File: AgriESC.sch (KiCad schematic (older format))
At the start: 129 parts, among them J1 SUPPLY, J10 GPIO, J11 USB_OTG, J12 HALL_ENC, J2 PH_A, J3 PH_B, J4 PH_C, J5 GND, J6 COMM, J7 SERVO, J8 CAN, J9 SWD, SW1 SW_SPDT, U1 FDMS7698, U10 STM32F405RGT6, U11 DRV8303, U12 TJA1051TK-3, U13 LMR16006YQ, U14 MCP1700-3302E_SOT23, U15 MCP1700-3302E_SOT23, U2 FDMS7698, U3 FDMS7698, U4 FDMS7698, U5 FDMS7698, U6 FDMS7698, U7 MAX9920, U8 MAX9920, U9 MAX9920, Y1 8M_15p_capacitance

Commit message: Created draft net
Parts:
- J1, J2, J3, J4, J5: footprint (none) -> Connector_Wire:SolderWirePad_1x01_SMD_5x10mm
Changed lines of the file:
@@
 F 0 "J2" H 820 -1625 50  0000 C CNN
 F 1 "PH_A" H 820 -1534 50  0000 C CNN
-F 2 "" H 900 -1400 50  0001 C CNN
+F 2 "Connector_Wire:SolderWirePad_1x01_SMD_5x10mm" H 900 -1400 50  0001 C CNN
 F 3 "~" H 900 -1400 50  0001 C CNN
 	1    900  -1400
@@
 F 0 "J3" H 4120 -1625 50  0000 C CNN
 F 1 "PH_B" H 4120 -1534 50  0000 C CNN
-F 2 "" H 4200 -1400 50  0001 C CNN
+F 2 "Connector_Wire:SolderWirePad_1x01_SMD_5x10mm" H 4200 -1400 50  0001 C CNN
 F 3 "~" H 4200 -1400 50  0001 C CNN
 	1    4200 -1400
@@
 F 0 "J4" H 7370 -1625 50  0000 C CNN
 F 1 "PH_C" H 7370 -1534 50  0000 C CNN
-F 2 "" H 7450 -1400 50  0001 C CNN
+F 2 "Connector_Wire:SolderWirePad_1x01_SMD_5x10mm" H 7450 -1400 50  0001 C CNN
 F 3 "~" H 7450 -1400 50  0001 C CNN
 	1    7450 -1400
@@
 F 0 "J1" H 10330 -2308 50  0000 L CNN
 F 1 "SUPPLY" H 10330 -2399 50  0000 L CNN
-F 2 "" H 10250 -2350 50  0001 C CNN
+F 2 "Connector_Wire:SolderWirePad_1x01_SMD_5x10mm" H 10250 -2350 50  0001 C CNN
 F 3 "~" H 10250 -2350 50  0001 C CNN
 	1    10250 -2350
@@
 F 0 "J5" H 10329 -158 50  0000 L CNN
 F 1 "GND" H 10329 -249 50  0000 L CNN
-F 2 "" H 10250 -200 50  0001 C CNN
+F 2 "Connector_Wire:SolderWirePad_1x01_SMD_5x10mm" H 10250 -200 50  0001 C CNN
 F 3 "~" H 10250 -200 50  0001 C CNN
 	1    10250 -200

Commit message: Updated schematic with new battery supply connector and more MPNs
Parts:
- removed J1: SUPPLY, Connector_Wire:SolderWirePad_1x01_SMD_5x10mm, symbol Connector_Generic:Conn_01x01
- removed J5: GND, Connector_Wire:SolderWirePad_1x01_SMD_5x10mm, symbol Connector_Generic:Conn_01x01
- removed Y1: 8M_15p_capacitance, Crystal:Crystal_HC49-U_Vertical, symbol Device:Crystal_GND3
- added J1: SUPPLY, AgriESC:XT30PW-M2, symbol Connector_Generic:Conn_01x02
- added Y1: 8M_15p_capacitance, Crystal:Crystal_HC49-U_Vertical, symbol Device:Crystal
- C10, C11, C12, C13, C14, C15, C16, C17, C18, C19, C20, C21, C22, C23, C24, C25, C26, C27, C28, C29, C30, C31, C32, C33, C34, C35, C36, C37, C38, C39, C40, C42, C43, C44, C45, C46, C48, C49, C50, C51, C52, C9: footprint Capacitor_SMD:C_0805_2012Metric_Pad1.15x1.40mm_HandSolder -> Capacitor_SMD:C_0603_1608Metric_Pad1.05x0.95mm_HandSolder
- C47: value 2u2_30V -> 2u2_35V; footprint Capacitor_SMD:C_0805_2012Metric_Pad1.15x1.40mm_HandSolder -> Capacitor_SMD:C_0603_1608Metric_Pad1.05x0.95mm_HandSolder
- D1, D2, D3: footprint LED_SMD:LED_0805_2012Metric_Pad1.15x1.40mm_HandSolder -> LED_SMD:LED_0603_1608Metric_Pad1.05x0.95mm_HandSolder
- J10, J12: footprint Connector_PinHeader_2.54mm:PinHeader_1x06_P2.54mm_Vertical -> AgriESC:JST_PA_01x06
- J11: footprint Connector_USB:USB_Micro-B_Amphenol_10103594-0001LF_Horizontal -> AgriESC:CONN-10118194-0001LF-FCI2
- J6: footprint Connector_PinHeader_2.54mm:PinHeader_1x08_P2.54mm_Vertical -> AgriESC:JST_PA_01x08
- J7: footprint Connector_PinHeader_2.54mm:PinHeader_1x03_P2.54mm_Vertical -> AgriESC:JST_PA_01x03
- J8: footprint Connector_PinHeader_2.54mm:PinHeader_1x04_P2.54mm_Vertical -> AgriESC:JST_PA_01x04
- J9: footprint Connector_PinHeader_2.54mm:PinHeader_1x05_P2.54mm_Vertical -> AgriESC:JST_PA_01x05
- R1, R10, R11, R12, R13, R14, R15, R16, R17, R18, R19, R2, R20, R21, R22, R23, R24, R25, R26, R27, R28, R29, R3, R30, R31, R32, R33, R34, R35, R36, R37, R38, R39, R40, R41, R42, R43, R7, R8, R9: footprint Resistor_SMD:R_0805_2012Metric_Pad1.15x1.40mm_HandSolder -> Resistor_SMD:R_0603_1608Metric_Pad1.05x0.95mm_HandSolder
- SW1: footprint AgriESC:1825232-1 -> Jumper:SolderJumper-3_P1.3mm_Open_RoundedPad1.0x1.5mm_NumberLabels
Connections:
- wire segments 595 -> 596
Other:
- note added: "35PX680MEFC10X16"
- note removed: "1825232-1"
- moved on the sheet: C46, C47, C48, C49, C50, C51, C52, D4, L1, R41, R42, R43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

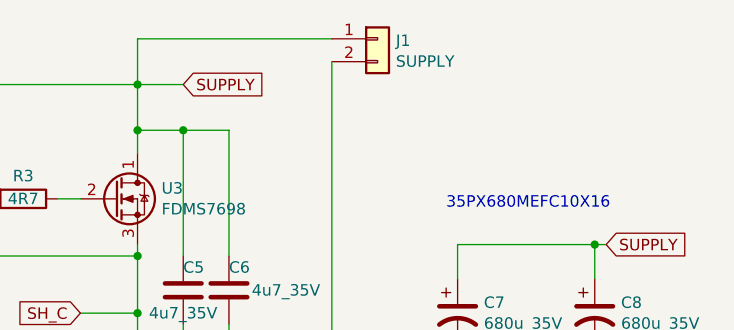
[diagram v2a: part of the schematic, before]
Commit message: Corrected battery connector polarity
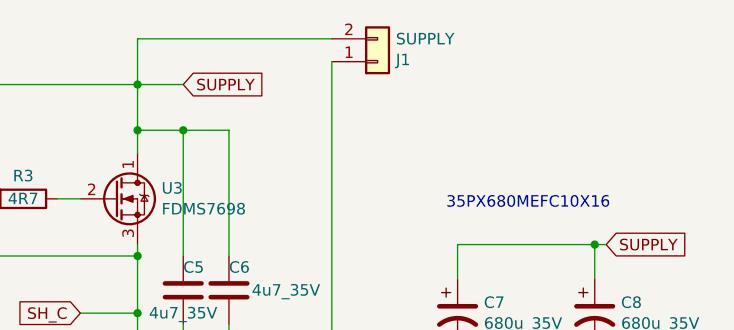
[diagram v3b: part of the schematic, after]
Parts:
- J1: footprint AgriESC:XT30PW-M2 -> AgriESC:XT30PW-F
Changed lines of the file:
@@
 L Connector_Generic:Conn_01x02 J1
 U 1 1 5C7BF897
-P 10900 -2350
-F 0 "J1" H 10980 -2358 50  0000 L CNN
-F 1 "SUPPLY" H 10980 -2449 50  0000 L CNN
-F 2 "AgriESC:XT30PW-M2" H 10900 -2350 50  0001 C CNN
-F 3 "~" H 10900 -2350 50  0001 C CNN
-	1    10900 -2350
-	1    0    0    -1
+P 10900 -2250
+F 0 "J1" H 10980 -2258 50  0000 L CNN
+F 1 "SUPPLY" H 10980 -2349 50  0000 L CNN
+F 2 "AgriESC:XT30PW-F" H 10900 -2250 50  0001 C CNN
+F 3 "~" H 10900 -2250 50  0001 C CNN
+	1    10900 -2250
+	1    0    0    1
 $EndComp
 Wire Wire Line

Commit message: Updated schematic with new components
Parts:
- removed Y1: 8M_15p_capacitance, Crystal:Crystal_HC49-U_Vertical, symbol Device:Crystal
- added Y1: 8M Resonator, AgriESC:CSTNE8M00G550000R0, symbol Device:Resonator
- L1: footprint Inductor_THT:L_Radial_D9.5mm_P5.00mm_Fastron_07HVP -> AgriESC:NR8040T220M
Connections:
- wire segments 596 -> 597
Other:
- note added: "CSTNE8M00G550000R0"
- note added: "NR8040T220M"
- note removed: "FC4STCBAF8.0-BAG200"
- note removed: "LHL08TB220K"
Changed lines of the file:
@@
 F 0 "L1" V 4490 9050 50  0000 C CNN
 F 1 "22u" V 4399 9050 50  0000 C CNN
-F 2 "Inductor_THT:L_Radial_D9.5mm_P5.00mm_Fastron_07HVP" H 4300 9050 50  0001 C CNN
+F 2 "AgriESC:NR8040T220M" H 4300 9050 50  0001 C CNN
 F 3 "~" H 4300 9050 50  0001 C CNN
 	1    4300 9050
@@
 $EndComp
 Text Notes 6550 2550 0    50   ~ 0
-FC4STCBAF8.0-BAG200
+CSTNE8M00G550000R0
 Text Notes 4100 8700 0    50   ~ 0
-LHL08TB220K
-$Comp
-L Device:Crystal Y1
-U 1 1 5C747901
-P 7000 2900
-F 0 "Y1" H 7000 3168 50  0000 C CNN
-F 1 "8M_15p_capacitance" H 7000 3077 50  0000 C CNN
-F 2 "Crystal:Crystal_HC49-U_Vertical" H 7000 2900 50  0001 C CNN
-F 3 "~" H 7000 2900 50  0001 C CNN
-	1    7000 2900
-	1    0    0    -1
-$EndComp
+NR8040T220M
 Text Notes 11200 -1600 0    50   ~ 0
 35PX680MEFC10X16
@@
 	10700 -200 10050 -200
 Connection ~ 10050 -200
+$Comp
+L Device:Resonator Y1
+U 1 1 5B759714
+P 7000 2900
+F 0 "Y1" H 7000 3148 50  0000 C CNN
+F 1 "8M Resonator" H 7000 3057 50  0000 C CNN
+F 2 "AgriESC:CSTNE8M00G550000R0" H 6975 2900 50  0001 C CNN
+F 3 "~" H 6975 2900 50  0001 C CNN
+	1    7000 2900
+	1    0    0    -1
+$EndComp
+$Comp
+L power:GND #PWR0101
+U 1 1 5B759B20
+P 7000 3150
+F 0 "#PWR0101" H 7000 2900 50  0001 C CNN
+F 1 "GND" H 7005 2977 50  0000 C CNN
+F 2 "" H 7000 3150 50  0001 C CNN
+F 3 "" H 7000 3150 50  0001 C CNN
+	1    7000 3150
+	1    0    0    -1
+$EndComp
+Wire Wire Line
+	7000 3100 7000 3150
 $EndSCHEMATC

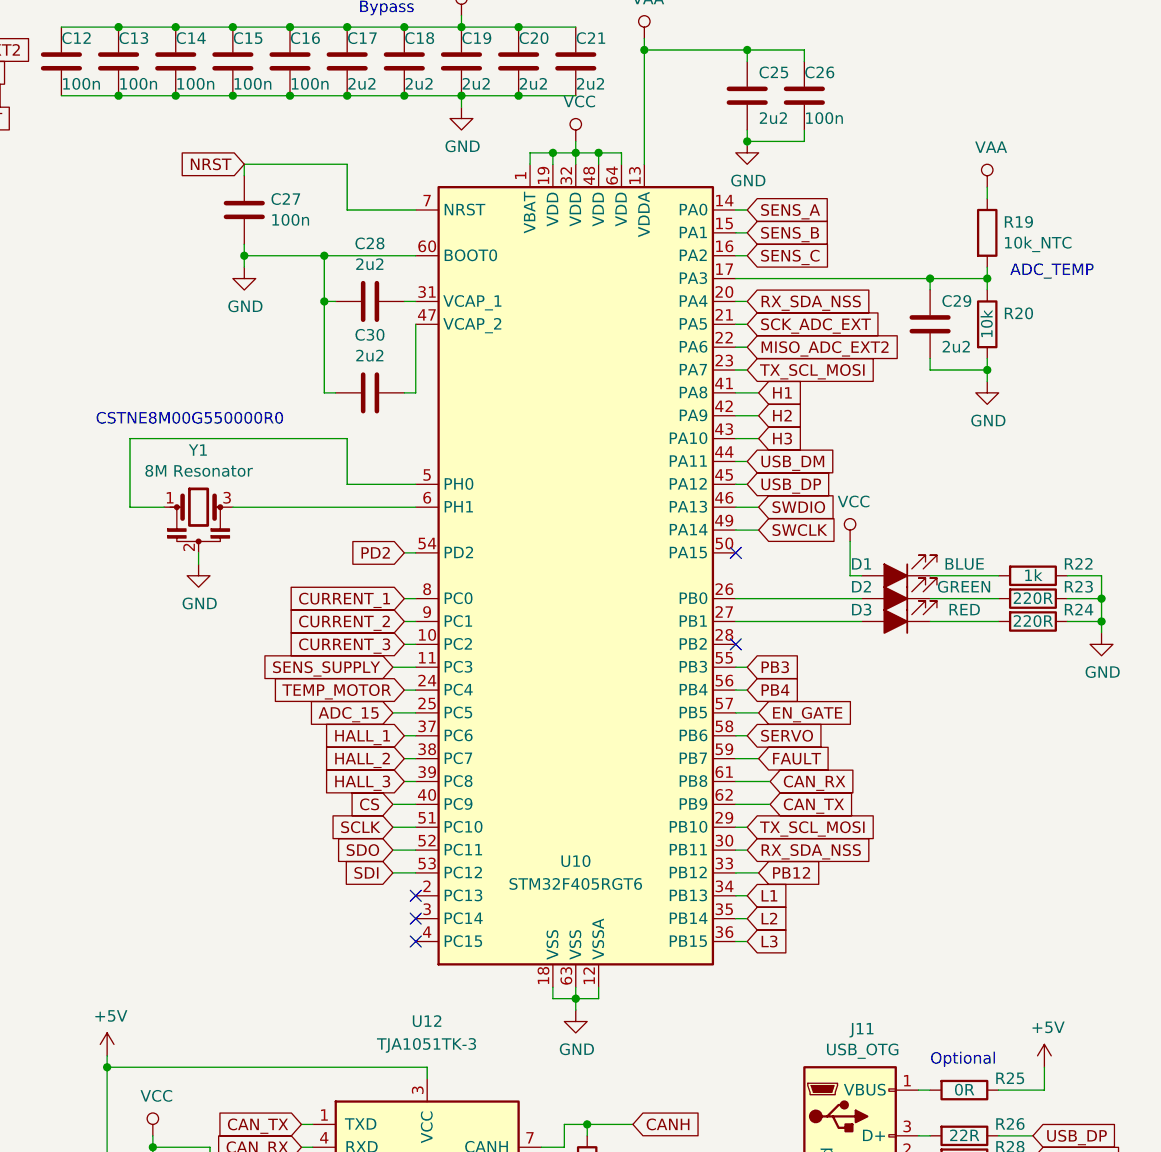
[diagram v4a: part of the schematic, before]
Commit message: Updated resonator footprint to include silkscreen
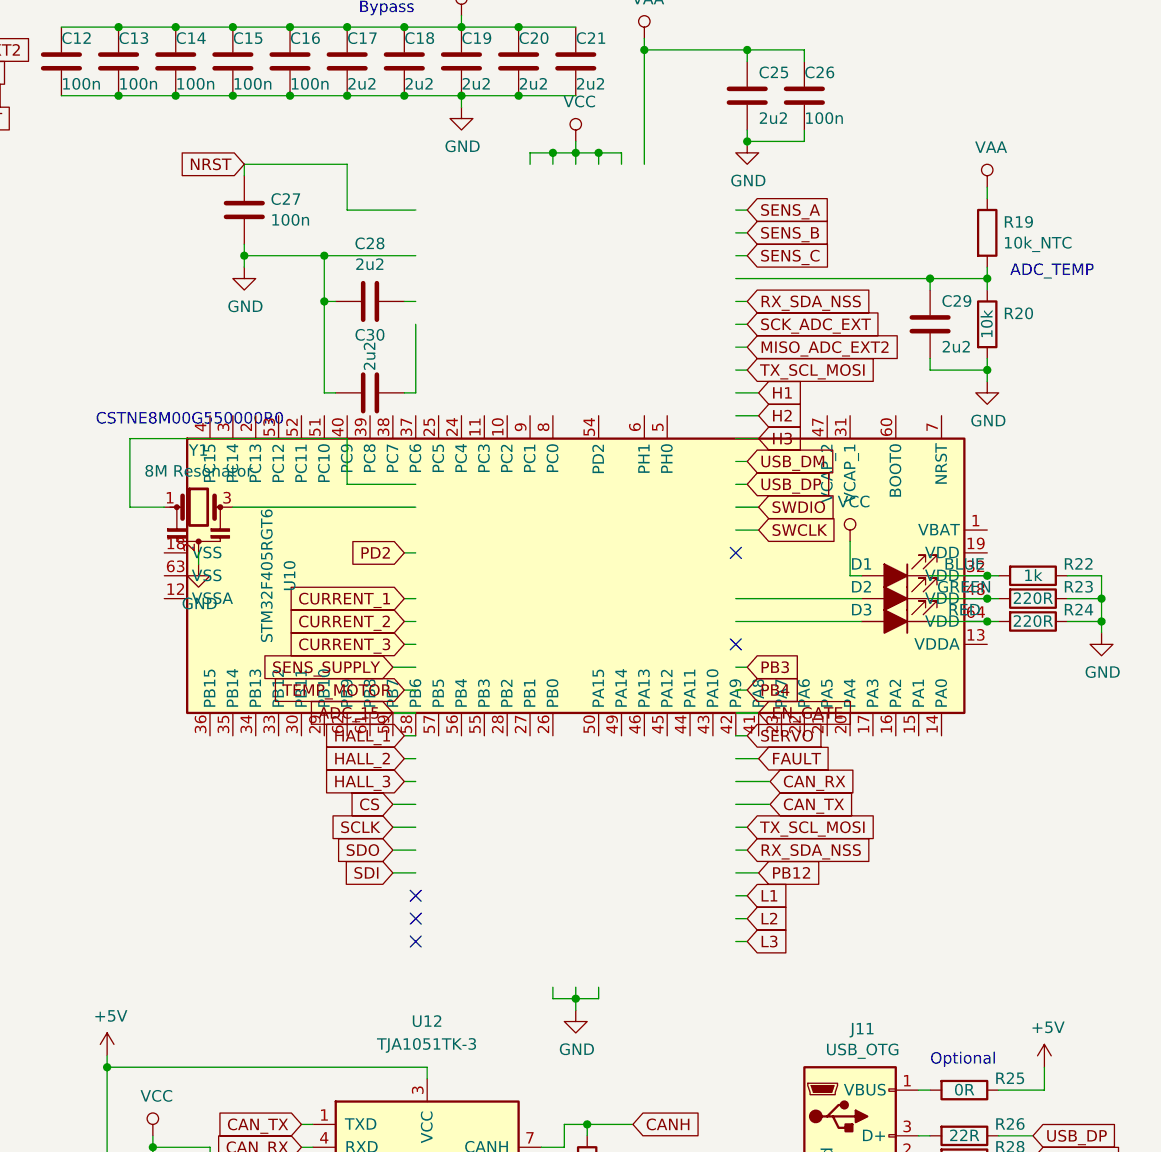
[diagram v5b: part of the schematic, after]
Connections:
- wire segments 597 -> 600
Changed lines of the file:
@@
 F 3 "http://www.st.com/st-web-ui/static/active/en/resource/technical/document/datasheet/DM00037051.pdf" H 8650 3200 50  0001 C CNN
 	1    8650 3200
-	1    0    0    -1
+	0    1    1    0
 $EndComp
 Wire Wire Line
@@
 P 7750 2400
 F 0 "C30" V 7498 2400 50  0000 C CNN
-F 1 "2u2" V 7589 2400 50  0000 C CNN
+F 1 "2u2" H 7589 2400 50  0000 C CNN
 F 2 "Capacitor_SMD:C_0603_1608Metric_Pad1.05x0.95mm_HandSolder" H 7788 2250 50  0001 C CNN
 F 3 "~" H 7750 2400 50  0001 C CNN
@@
 	9850 3200 9900 3200
 Wire Wire Line
-	10500 3200 10200 3200
+	10500 3200 10450 3200
 Wire Wire Line
 	9350 3300 9900 3300
@@
 $EndComp
 Wire Wire Line
-	10500 3300 10200 3300
+	10500 3300 10450 3300
 Wire Wire Line
-	10200 3400 10500 3400
+	10200 3400 10450 3400
 Wire Wire Line
 	10800 3200 10950 3200
@@
 Wire Wire Line
 	7000 3100 7000 3150
+Connection ~ 10450 3200
+Wire Wire Line
+	10450 3200 10200 3200
+Connection ~ 10450 3300
+Wire Wire Line
+	10450 3300 10200 3300
+Connection ~ 10450 3400
+Wire Wire Line
+	10450 3400 10500 3400
 $EndSCHEMATC

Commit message: Fix to schematic
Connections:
- wire segments 600 -> 597
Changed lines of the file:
@@
 F 3 "http://www.st.com/st-web-ui/static/active/en/resource/technical/document/datasheet/DM00037051.pdf" H 8650 3200 50  0001 C CNN
 	1    8650 3200
-	0    1    1    0
+	1    0    0    -1
 $EndComp
 Wire Wire Line
@@
 	9450 2400 9350 2400
 Wire Wire Line
-	9350 2500 9450 2500
-Wire Wire Line
 	9350 2600 9450 2600
 Text GLabel 9400 2700 2    50   Input ~ 0
@@
 	7950 2000 7900 2000
 Wire Wire Line
-	7950 2100 7950 2400
-Wire Wire Line
 	7950 2400 7900 2400
 Wire Wire Line
@@
 	9850 3200 9900 3200
 Wire Wire Line
-	10500 3200 10450 3200
-Wire Wire Line
 	9350 3300 9900 3300
 Wire Wire Line
@@
 $EndComp
 Wire Wire Line
-	10500 3300 10450 3300
-Wire Wire Line
-	10200 3400 10450 3400
-Wire Wire Line
 	10800 3200 10950 3200
 Wire Wire Line
@@
 Wire Wire Line
 	7000 3100 7000 3150
-Connection ~ 10450 3200
 Wire Wire Line
-	10450 3200 10200 3200
-Connection ~ 10450 3300
+	9350 2500 9450 2500
+Wire Wire Line
+	7950 2100 7950 2400
+Wire Wire Line
+	10200 3400 10500 3400
 Wire Wire Line
-	10450 3300 10200 3300
-Connection ~ 10450 3400
+	10200 3300 10500 3300
 Wire Wire Line
-	10450 3400 10500 3400
+	10200 3200 10500 3200
 $EndSCHEMATC

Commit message: Before CAN package update
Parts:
- U12: footprint Package_DFN_QFN:DFN-8-1EP_3x3mm_P0.65mm_EP1.55x2.4mm -> Housings_DFN_QFN:DFN-8-1EP_3x3mm_Pitch0.65mm
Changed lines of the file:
@@
 EESchema Schematic File Version 4
 LIBS:AgriESC-cache
-EELAYER 26 0
+EELAYER 29 0
 EELAYER END
 $Descr A4 11693 8268
@@
 F 0 "U12" H 8000 6450 50  0000 C CNN
 F 1 "TJA1051TK-3" H 8000 6350 50  0000 C CNN
-F 2 "Package_DFN_QFN:DFN-8-1EP_3x3mm_P0.65mm_EP1.55x2.4mm" H 8000 5300 50  0001 C CIN
+F 2 "Housings_DFN_QFN:DFN-8-1EP_3x3mm_Pitch0.65mm" H 8000 5300 50  0001 C CIN
 F 3 "http://www.nxp.com/documents/data_sheet/TJA1051.pdf" H 8000 5800 50  0001 C CNN
 	1    8000 5800

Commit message: Version 1.0 completed
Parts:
- added NT1, NT2, NT3: Net-Tie_2, NetTie:NetTie-2_SMD_Pad0.5mm, symbol Device:Net-Tie_2
- C7, C8: footprint Capacitor_THT:CP_Radial_D10.0mm_P5.00mm -> AgriESC:CP_Radial_D10.0mm_P5.00mm_Side_Mounted
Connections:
- net GND: now also NT1.1, NT2.1, NT3.1; no longer U11.30 (SL_C), U11.35 (SL_B), U11.40 (SL_A)
- net VCC: now also J12.6 (Pin_6), R33.2, R34.2, R37.2, SW1.2 (B)
- new net SL_A: NT1.2, U11.40 (SL_A)
- new net SL_B: NT2.2, U11.35 (SL_B)
- new net SL_C: NT3.2, U11.30 (SL_C)
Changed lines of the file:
@@
 EESchema Schematic File Version 4
 LIBS:AgriESC-cache
-EELAYER 29 0
+EELAYER 26 0
 EELAYER END
 $Descr A4 11693 8268
@@
 SL_A
 Wire Wire Line
-	3050 -450 3300 -450
-Wire Wire Line
 	3300 -450 3300 -600
 $Comp
@@
 	3300 -1950 3300 -2150
 Connection ~ 3300 -1950
-Wire Wire Line
-	3300 -450 3300 -200
 Text GLabel 2500 -1650 0    50   Input ~ 0
 GH_A
@@
 SL_B
 Wire Wire Line
-	6350 -450 6600 -450
-Wire Wire Line
 	6600 -450 6600 -600
 $Comp
@@
 	6600 -1950 6600 -2150
 Connection ~ 6600 -1950
-Wire Wire Line
-	6600 -450 6600 -200
 Text GLabel 5800 -1650 0    50   Input ~ 0
 GH_B
@@
 SL_C
 Wire Wire Line
-	9600 -450 9850 -450
-Wire Wire Line
 	9850 -450 9850 -600
 $Comp
@@
 	9850 -2350 9850 -2150
 Wire Wire Line
-	3300 -200 6600 -200
-Connection ~ 6600 -200
-Wire Wire Line
-	9850 -450 9850 -200
-Wire Wire Line
 	10050 -200 10050 -50
-Connection ~ 9850 -200
-Wire Wire Line
-	9850 -200 10050 -200
-Wire Wire Line
-	6600 -200 9850 -200
 Text GLabel 1050 800  0    50   Input ~ 0
 CURRENT_1
@@
 L power:PWR_FLAG #FLG01
 U 1 1 5E04539D
-P 2650 6800
-F 0 "#FLG01" H 2650 6875 50  0001 C CNN
-F 1 "PWR_FLAG" H 2650 6974 50  0000 C CNN
-F 2 "" H 2650 6800 50  0001 C CNN
-F 3 "~" H 2650 6800 50  0001 C CNN
-	1    2650 6800
+P 2700 6200
+F 0 "#FLG01" H 2700 6275 50  0001 C CNN
+F 1 "PWR_FLAG" H 2700 6374 50  0000 C CNN
+F 2 "" H 2700 6200 50  0001 C CNN
+F 3 "~" H 2700 6200 50  0001 C CNN
+	1    2700 6200
 	1    0    0    -1
 $EndComp
@@
 L power:GND #PWR055
 U 1 1 5E045557
-P 2650 6850
-F 0 "#PWR055" H 2650 6600 50  0001 C CNN
-F 1 "GND" H 2655 6677 50  0000 C CNN
-F 2 "" H 2650 6850 50  0001 C CNN
-F 3 "" H 2650 6850 50  0001 C CNN
-	1    2650 6850
+P 2700 6250
+F 0 "#PWR055" H 2700 6000 50  0001 C CNN
+F 1 "GND" H 2705 6077 50  0000 C CNN
+F 2 "" H 2700 6250 50  0001 C CNN
+F 3 "" H 2700 6250 50  0001 C CNN
+	1    2700 6250
 	1    0    0    -1
 $EndComp
@@
 L power:PWR_FLAG #FLG02
 U 1 1 5E0457CD
-P 3000 6850
-F 0 "#FLG02" H 3000 6925 50  0001 C CNN
-F 1 "PWR_FLAG" H 3000 7023 50  0000 C CNN
-F 2 "" H 3000 6850 50  0001 C CNN
-F 3 "~" H 3000 6850 50  0001 C CNN
-	1    3000 6850
+P 3050 6250
+F 0 "#FLG02" H 3050 6325 50  0001 C CNN
+F 1 "PWR_FLAG" H 3050 6423 50  0000 C CNN
+F 2 "" H 3050 6250 50  0001 C CNN
+F 3 "~" H 3050 6250 50  0001 C CNN
+	1    3050 6250
 	-1   0    0    1
 $EndComp
@@
 L power:+5V #PWR054
 U 1 1 5E045EB9
-P 3000 6800
-F 0 "#PWR054" H 3000 6650 50  0001 C CNN
-F 1 "+5V" H 3015 6973 50  0000 C CNN
-F 2 "" H 3000 6800 50  0001 C CNN
-F 3 "" H 3000 6800 50  0001 C CNN
-	1    3000 6800
+P 3050 6200
+F 0 "#PWR054" H 3050 6050 50  0001 C CNN
+F 1 "+5V" H 3065 6373 50  0000 C CNN
+F 2 "" H 3050 6200 50  0001 C CNN
+F 3 "" H 3050 6200 50  0001 C CNN
+	1    3050 6200
 	1    0    0    -1
 $EndComp
 Wire Wire Line
-	3000 6800 3000 6850
+	3050 6200 3050 6250
 Wire Wire Line
-	2650 6800 2650 6850
+	2700 6200 2700 6250
 Text GLabel 1850 8850 0    50   Input ~ 0
 SUPPLY
@@
 L power:PWR_FLAG #FLG03
 U 1 1 5E1F88B7
-P 3400 6850
-F 0 "#FLG03" H 3400 6925 50  0001 C CNN
-F 1 "PWR_FLAG" H 3400 7023 50  0000 C CNN
-F 2 "" H 3400 6850 50  0001 C CNN
-F 3 "~" H 3400 6850 50  0001 C CNN
-	1    3400 6850
+P 2700 7050
+F 0 "#FLG03" H 2700 7125 50  0001 C CNN
+F 1 "PWR_FLAG" H 2700 7223 50  0000 C CNN
+F 2 "" H 2700 7050 50  0001 C CNN
+F 3 "~" H 2700 7050 50  0001 C CNN
+	1    2700 7050
 	-1   0    0    1
 $EndComp
-Text GLabel 3400 6800 1    50   Input ~ 0
+Text GLabel 2700 7000 1    50   Input ~ 0
 SUPPLY
 Wire Wire Line
-	3400 6800 3400 6850
+	2700 7000 2700 7050
 Text Notes 2550 9900 0    50   ~ 0
 From the design guide
@@
 F 0 "C7" H 11365 -1104 50  0000 L CNN
 F 1 "680u_35V" H 11365 -1195 50  0000 L CNN
-F 2 "Capacitor_THT:CP_Radial_D10.0mm_P5.00mm" H 11250 -1150 50  0001 C CNN
+F 2 "AgriESC:CP_Radial_D10.0mm_P5.00mm_Side_Mounted" H 11250 -1150 50  0001 C CNN
 F 3 "~" H 11250 -1150 50  0001 C CNN
 	1    11250 -1150
@@
 F 0 "C8" H 11965 -1104 50  0000 L CNN
 F 1 "680u_35V" H 11965 -1195 50  0000 L CNN
-F 2 "Capacitor_THT:CP_Radial_D10.0mm_P5.00mm" H 11850 -1150 50  0001 C CNN
+F 2 "AgriESC:CP_Radial_D10.0mm_P5.00mm_Side_Mounted" H 11850 -1150 50  0001 C CNN
 F 3 "~" H 11850 -1150 50  0001 C CNN
 	1    11850 -1150
@@
 Wire Wire Line
 	10200 3200 10500 3200
+$Comp
+L Device:Net-Tie_2 NT2
+U 1 1 5C1B6C66
+P 6500 -450
+F 0 "NT2" H 6500 -628 50  0000 C CNN
+F 1 "Net-Tie_2" H 6500 -537 50  0000 C CNN
+F 2 "NetTie:NetTie-2_SMD_Pad0.5mm" H 6500 -450 50  0001 C CNN
+F 3 "~" H 6500 -450 50  0001 C CNN
+	1    6500 -450
+	-1   0    0    1
+$EndComp
+$Comp
+L Device:Net-Tie_2 NT3
+U 1 1 5C1B70D1
+P 9750 -450
+F 0 "NT3" H 9750 -628 50  0000 C CNN
+F 1 "Net-Tie_2" H 9750 -537 50  0000 C CNN
+F 2 "NetTie:NetTie-2_SMD_Pad0.5mm" H 9750 -450 50  0001 C CNN
+F 3 "~" H 9750 -450 50  0001 C CNN
+	1    9750 -450
+	-1   0    0    1
+$EndComp
+$Comp
+L Device:Net-Tie_2 NT1
+U 1 1 5C1B74C5
+P 3200 -450
+F 0 "NT1" H 3200 -628 50  0000 C CNN
+F 1 "Net-Tie_2" H 3200 -537 50  0000 C CNN
+F 2 "NetTie:NetTie-2_SMD_Pad0.5mm" H 3200 -450 50  0001 C CNN
+F 3 "~" H 3200 -450 50  0001 C CNN
+	1    3200 -450
+	-1   0    0    1
+$EndComp
+Wire Wire Line
+	3100 -450 3050 -450
+Wire Wire Line
+	3300 -450 3300 -200
+Wire Wire Line
+	6400 -450 6350 -450
+Wire Wire Line
+	3300 -200 6600 -200
+Wire Wire Line
+	6600 -450 6600 -200
+Connection ~ 6600 -200
+Wire Wire Line
+	9650 -450 9600 -450
+Wire Wire Line
+	6600 -200 9850 -200
+Wire Wire Line
+	9850 -450 9850 -200
+Connection ~ 9850 -200
+Wire Wire Line
+	9850 -200 10050 -200
+Wire Wire Line
+	4300 6350 4350 6350
+Connection ~ 4350 6350
+$Comp
+L power:VCC #PWR0102
+U 1 1 5C9F451C
+P 3050 6800
+F 0 "#PWR0102" H 3050 6650 50  0001 C CNN
+F 1 "VCC" H 3067 6973 50  0000 C CNN
+F 2 "" H 3050 6800 50  0001 C CNN
+F 3 "" H 3050 6800 50  0001 C CNN
+	1    3050 6800
+	1    0    0    -1
+$EndComp
+Wire Wire Line
+	3050 6800 3050 6850
+Text Label 3050 6850 3    50   ~ 0
+HALL_POWER
+Text Label 4300 6350 2    50   ~ 0
+HALL_POWER
 $EndSCHEMATC
